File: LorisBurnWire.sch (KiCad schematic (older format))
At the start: 54 parts, among them J1 BurnWire, J2 BurnWire, J3 BurnWire, J4 BurnWire, Q1 BUK7M6R3-40EX, Q2 BUK7M6R3-40EX, Q3 BUK7M6R3-40EX, Q4 BUK7M6R3-40EX, U1 TLC555ID, U2 TLC555ID, U3 LP38501-ADJ, U4 TLC555ID, U5 LMP8646, U6 TLC555ID

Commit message: Added footprint to LMP8646
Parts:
- U5: footprint (none) -> TempoFootprints:SOT-23-THN (DDC)
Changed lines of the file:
@@
 F 0 "U5" H 8200 2000 50  0000 R CNN
 F 1 "LMP8646" H 8300 1925 50  0000 R CNN
-F 2 "" H 8150 1850 50  0001 C CNN
+F 2 "TempoFootprints:SOT-23-THN (DDC)" H 8150 1850 50  0001 C CNN
 F 3 "" H 8150 1850 50  0001 C CNN
 	1    8150 1900

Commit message: added 5v regulator and finished adding footprints
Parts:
- added C16, C17, C18, C19: 22u, Capacitor_SMD:C_1206_3216Metric_Pad1.42x1.75mm_HandSolder, symbol Device:C_Small
- added L1: L_Small, BurnWire:SPM6530T-3R3M, symbol Device:L_Small
- added R22, R24: 100k, Resistor_SMD:R_1206_3216Metric_Pad1.42x1.75mm_HandSolder, symbol Device:R_Small
- added R23: 909k, Resistor_SMD:R_1206_3216Metric_Pad1.42x1.75mm_HandSolder, symbol Device:R_Small
- added U7: RT4812, Package_TO_SOT_SMD:TSOT-23-8_HandSoldering, symbol BurnWireLib:RT4812
- JP1: footprint TempoFootprints:TE_87224-3 -> Connector_PinHeader_2.54mm:PinHeader_1x03_P2.54mm_Vertical
- U3: footprint (none) -> TO_SOT_Packages_SMD:TO-263-5_TabPin3
- U5: footprint TempoFootprints:SOT-23-THN (DDC) -> TO_SOT_Packages_SMD:TSOT-23-6_HandSoldering
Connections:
- net labels removed: 3.5V
- wire segments 219 -> 262
- no-connect marks 0 -> 1
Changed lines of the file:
@@
 F 0 "U3" H 5975 2240 50  0000 C CNN
 F 1 "LP38501-ADJ" H 5975 2149 50  0000 C CNN
-F 2 "" H 5900 2225 50  0001 C CNN
+F 2 "TO_SOT_Packages_SMD:TO-263-5_TabPin3" H 5900 2225 50  0001 C CNN
 F 3 "" H 5900 2225 50  0001 C CNN
 	1    5900 1775
 	1    0    0    -1
 $EndComp
-Wire Wire Line
-	5550 1725 5350 1725
 $Comp
 L Device:C_Small C8
@@
 F 0 "U5" H 8200 2000 50  0000 R CNN
 F 1 "LMP8646" H 8300 1925 50  0000 R CNN
-F 2 "TempoFootprints:SOT-23-THN (DDC)" H 8150 1850 50  0001 C CNN
+F 2 "TO_SOT_Packages_SMD:TSOT-23-6_HandSoldering" H 8150 1850 50  0001 C CNN
 F 3 "" H 8150 1850 50  0001 C CNN
 	1    8150 1900
@@
 Wire Wire Line
 	6775 7850 9125 7850
-Text Label 6650 1575 1    50   ~ 0
-3.5V
 Wire Notes Line
 	10950 700  625  700
@@
 F 0 "JP1" H 5600 2000 50  0000 C CNN
 F 1 "Jumper_3_Open" H 5675 2075 50  0000 C CNN
-F 2 "TempoFootprints:TE_87224-3" H 5350 1875 50  0001 C CNN
+F 2 "Connector_PinHeader_2.54mm:PinHeader_1x03_P2.54mm_Vertical" H 5350 1875 50  0001 C CNN
 F 3 "~" H 5350 1875 50  0001 C CNN
 	1    5350 1875
@@
 Wire Wire Line
 	2350 7850 2350 8150
+$Comp
+L BurnWireLib:RT4812 U7
+U 1 1 5EAF5CE4
+P 2225 1975
+F 0 "U7" H 2275 2390 50  0000 C CNN
+F 1 "RT4812" H 2275 2299 50  0000 C CNN
+F 2 "Package_TO_SOT_SMD:TSOT-23-8_HandSoldering" H 2275 2275 50  0001 C CNN
+F 3 "https://www.digikey.ca/product-detail/en/richtek-usa-inc/RT4812GJ8F/1028-1512-1-ND/5640521" H 2275 2275 50  0001 C CNN
+	1    2225 1975
+	1    0    0    -1
+$EndComp
+$Comp
+L Device:C_Small C16
+U 1 1 5EAF69B3
+P 1425 2000
+F 0 "C16" H 1225 2025 50  0000 L CNN
+F 1 "22u" H 1175 1950 50  0000 L CNN
+F 2 "Capacitor_SMD:C_1206_3216Metric_Pad1.42x1.75mm_HandSolder" H 1425 2000 50  0001 C CNN
+F 3 "~" H 1425 2000 50  0001 C CNN
+	1    1425 2000
+	1    0    0    -1
+$EndComp
+$Comp
+L Device:L_Small L1
+U 1 1 5EB25078
+P 1575 1825
+F 0 "L1" V 1760 1825 50  0000 C CNN
+F 1 "L_Small" V 1669 1825 50  0000 C CNN
+F 2 "BurnWire:SPM6530T-3R3M" H 1575 1825 50  0001 C CNN
+F 3 "~" H 1575 1825 50  0001 C CNN
+F 4 "RICHTEK" H 1575 1825 50  0001 C CNN "MFG Name"
+F 5 "SPM6530T-3R3M" H 1575 1825 50  0001 C CNN "MFG Part Number"
+	1    1575 1825
+	0    -1   -1   0
+$EndComp
+Wire Wire Line
+	1675 1825 1875 1825
+NoConn ~ 1875 2375
+Wire Wire Line
+	1425 1825 1475 1825
+Wire Wire Line
+	1425 1900 1425 1875
+Wire Wire Line
+	1875 2025 1600 2025
+Wire Wire Line
+	1600 2025 1600 1875
+Wire Wire Line
+	1600 1875 1550 1875
+Connection ~ 1425 1875
+Wire Wire Line
+	1425 1875 1425 1825
+$Comp
+L Device:C_Small C17
+U 1 1 5ECA27CF
+P 1550 2175
+F 0 "C17" H 1650 2200 50  0000 L CNN
+F 1 "22u" H 1650 2125 50  0000 L CNN
+F 2 "Capacitor_SMD:C_1206_3216Metric_Pad1.42x1.75mm_HandSolder" H 1550 2175 50  0001 C CNN
+F 3 "~" H 1550 2175 50  0001 C CNN
+	1    1550 2175
+	1    0    0    -1
+$EndComp
+Wire Wire Line
+	1550 2075 1550 1875
+Connection ~ 1550 1875
+Wire Wire Line
+	1550 1875 1425 1875
+Wire Wire Line
+	1550 2275 1550 2725
+Wire Wire Line
+	2325 2725 2325 2625
+Wire Wire Line
+	2275 2575 2275 2625
+Wire Wire Line
+	2275 2625 2325 2625
+Wire Wire Line
+	2375 2575 2375 2625
+Wire Wire Line
+	2375 2625 2325 2625
+Connection ~ 2325 2625
+Wire Wire Line
+	1425 2100 1425 2725
+Wire Wire Line
+	1425 2725 1550 2725
+Connection ~ 1550 2725
+Wire Wire Line
+	1550 2725 1675 2725
+$Comp
+L Device:R_Small R22
+U 1 1 5ED0112A
+P 1675 2500
+F 0 "R22" H 1734 2546 50  0000 L CNN
+F 1 "100k" H 1725 2475 50  0000 L CNN
+F 2 "Resistor_SMD:R_1206_3216Metric_Pad1.42x1.75mm_HandSolder" H 1675 2500 50  0001 C CNN
+F 3 "~" H 1675 2500 50  0001 C CNN
+	1    1675 2500
+	1    0    0    -1
+$EndComp
+Wire Wire Line
+	1675 2400 1675 2275
+Wire Wire Line
+	1675 2275 1875 2275
+Wire Wire Line
+	1675 2600 1675 2725
+Connection ~ 1675 2725
+Wire Wire Line
+	1675 2725 2325 2725
+Wire Wire Line
+	1425 1825 1225 1825
+Connection ~ 1425 1825
+Text GLabel 1225 1825 0    50   Input ~ 0
+PACK+
+$Comp
+L Device:R_Small R23
+U 1 1 5ED480F4
+P 2775 2050
+F 0 "R23" H 2834 2096 50  0000 L CNN
+F 1 "909k" H 2825 2025 50  0000 L CNN
+F 2 "Resistor_SMD:R_1206_3216Metric_Pad1.42x1.75mm_HandSolder" H 2775 2050 50  0001 C CNN
+F 3 "~" H 2775 2050 50  0001 C CNN
+	1    2775 2050
+	1    0    0    -1
+$EndComp
+$Comp
+L Device:R_Small R24
+U 1 1 5ED58F71
+P 2775 2400
+F 0 "R24" H 2834 2446 50  0000 L CNN
+F 1 "100k" H 2825 2375 50  0000 L CNN
+F 2 "Resistor_SMD:R_1206_3216Metric_Pad1.42x1.75mm_HandSolder" H 2775 2400 50  0001 C CNN
+F 3 "~" H 2775 2400 50  0001 C CNN
+	1    2775 2400
+	1    0    0    -1
+$EndComp
+Wire Wire Line
+	2675 1875 2775 1875
+Wire Wire Line
+	2775 1875 2775 1950
+Wire Wire Line
+	2675 2225 2775 2225
+Wire Wire Line
+	2775 2225 2775 2150
+Wire Wire Line
+	2775 2225 2775 2300
+Connection ~ 2775 2225
+Wire Wire Line
+	2775 2500 2775 2725
+Wire Wire Line
+	2775 2725 2325 2725
+Connection ~ 2325 2725
+Connection ~ 2775 1875
+$Comp
+L Device:C_Small C18
+U 1 1 5EDF6398
+P 3175 2175
+F 0 "C18" H 3275 2175 50  0000 L CNN
+F 1 "22u" H 3275 2100 50  0000 L CNN
+F 2 "Capacitor_SMD:C_1206_3216Metric_Pad1.42x1.75mm_HandSolder" H 3175 2175 50  0001 C CNN
+F 3 "~" H 3175 2175 50  0001 C CNN
+	1    3175 2175
+	1    0    0    -1
+$EndComp
+$Comp
+L Device:C_Small C19
+U 1 1 5EE2E4CA
+P 3500 2175
+F 0 "C19" H 3600 2175 50  0000 L CNN
+F 1 "22u" H 3600 2100 50  0000 L CNN
+F 2 "Capacitor_SMD:C_1206_3216Metric_Pad1.42x1.75mm_HandSolder" H 3500 2175 50  0001 C CNN
+F 3 "~" H 3500 2175 50  0001 C CNN
+	1    3500 2175
+	1    0    0    -1
+$EndComp
+Wire Wire Line
+	3175 2000 3175 2075
+Wire Wire Line
+	3500 2000 3500 2075
+Wire Wire Line
+	3175 2275 3175 2450
+Wire Wire Line
+	3500 2450 3500 2275
+Connection ~ 2775 2725
+$Comp
+L power:+5V #PWR0101
+U 1 1 5EECD4F8
+P 3700 1875
+F 0 "#PWR0101" H 3700 1725 50  0001 C CNN
+F 1 "+5V" H 3715 2048 50  0000 C CNN
+F 2 "" H 3700 1875 50  0001 C CNN
+F 3 "" H 3700 1875 50  0001 C CNN
+	1    3700 1875
+	1    0    0    -1
+$EndComp
+Wire Wire Line
+	5350 1725 5550 1725
+Wire Wire Line
+	2775 1875 3325 1875
+Wire Wire Line
+	3175 2000 3325 2000
+Wire Wire Line
+	3175 2450 3325 2450
+Wire Wire Line
+	3325 2450 3325 2725
+Connection ~ 3325 2450
+Wire Wire Line
+	3325 2450 3500 2450
+Wire Wire Line
+	3325 2725 2775 2725
+Wire Wire Line
+	3325 2000 3325 1875
+Connection ~ 3325 2000
+Connection ~ 3325 1875
+Wire Wire Line
+	3325 2000 3500 2000
+Wire Wire Line
+	3325 1875 3700 1875
+$Comp
+L power:GND #PWR0102
+U 1 1 5EF9B6AD
+P 2325 2725
+F 0 "#PWR0102" H 2325 2475 50  0001 C CNN
+F 1 "GND" H 2330 2552 50  0000 C CNN
+F 2 "" H 2325 2725 50  0001 C CNN
+F 3 "" H 2325 2725 50  0001 C CNN
+	1    2325 2725
+	1    0    0    -1
+$EndComp
 $EndSCHEMATC

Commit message: Initial work on PCB layout
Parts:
- D1, D2, D3: footprint Diodes_SMD:D_SOD-123 -> Diode_SMD:D_SOD-123
- U1, U2, U4, U6: footprint Housings_SOIC:SOIC-8_3.9x4.9mm_Pitch1.27mm -> Package_SO:SOIC-8_3.9x4.9mm_P1.27mm
- U3: footprint TO_SOT_Packages_SMD:TO-263-5_TabPin3 -> Package_TO_SOT_SMD:TO-263-5_TabPin3
- U5: footprint TO_SOT_Packages_SMD:TSOT-23-6_HandSoldering -> Package_TO_SOT_SMD:TSOT-23-6_HandSoldering
- U7: symbol BurnWireLib:RT4812 -> LorisBurnWire-rescue:RT4812-BurnWireLib

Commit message: Rough layout of PCB
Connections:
- net PWR_FLAG: now reaches J1.1 (Pin_1), J2.1 (Pin_1), J3.1 (Pin_1), J4.1 (Pin_1)
- net PWR_FLAG: now also R15.1, R18.1, U5.4 (IN-)
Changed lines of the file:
@@
 	1    0    0    -1
 $EndComp
+Text GLabel 9950 1550 3    50   Input ~ 0
+PWR_FLAG
+Text GLabel 5750 7850 3    50   Input ~ 0
+PWR_FLAG
 $EndSCHEMATC

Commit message: edits
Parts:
- added J5: TimerTestPoints, Connector_PinHeader_2.54mm:PinHeader_1x04_P2.54mm_Vertical, symbol Connector:Conn_01x04_Male
- added J6: PACK+, TempoFootprints:TE_282837-2, symbol Connector:Screw_Terminal_01x02
- added J7: TestPointCurrentLimiter, Connector_PinHeader_2.54mm:PinHeader_1x02_P2.54mm_Vertical, symbol Connector:Conn_01x02_Male
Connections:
- net GND: now also J6.2 (Pin_2)
- net PACK+: now also J6.1 (Pin_1)
- net WireCutter1: now also J5.1 (Pin_1)
- net WireCutter2: now also J5.2 (Pin_2)
- net WireCutter3: now also J5.3 (Pin_3)
- net WireCutter4: now also J5.4 (Pin_4)
- net OUT: now reaches C8.2, R18.2, U3.4 (OUT), U5.3 (+IN)
- net OUT: now also J7.2 (Pin_2)
- net PWR_FLAG renamed VS
- net VS: now also J7.1 (Pin_1)
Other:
- moved on the sheet: C1, C10, C11, C14, C16, C17, C18, C19, C2, C3, C4, C5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

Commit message: added simulation
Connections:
- net GND: now also C16.1; no longer C16.2
- net PACK+: now also C16.2, R22.1, U7.7 (EN); no longer C16.1
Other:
- moved on the sheet: C16, C17
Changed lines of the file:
@@
-$EndComp
-$Comp
-L Device:C_Small C16
-U 1 1 5EAF69B3
-P 1425 1725
-F 0 "C16" H 1225 1750 50  0000 L CNN
-F 1 "22u" H 1175 1675 50  0000 L CNN
-F 2 "Capacitor_SMD:C_1206_3216Metric_Pad1.42x1.75mm_HandSolder" H 1425 1725 50  0001 C CNN
-F 3 "~" H 1425 1725 50  0001 C CNN
-	1    1425 1725
-	1    0    0    -1
 $EndComp
 $Comp
@@
 U 1 1 5EB25078
 P 1575 1550
-F 0 "L1" V 1760 1550 50  0000 C CNN
-F 1 "L_Small" V 1669 1550 50  0000 C CNN
+F 0 "L1" V 1750 1475 50  0000 C CNN
+F 1 "L_Small" V 1650 1450 50  0000 C CNN
 F 2 "BurnWire:SPM6530T-3R3M" H 1575 1550 50  0001 C CNN
 F 3 "~" H 1575 1550 50  0001 C CNN
@@
 	1675 1550 1875 1550
 NoConn ~ 1875 2100
-Wire Wire Line
-	1425 1550 1475 1550
-Wire Wire Line
-	1425 1625 1425 1600
-Wire Wire Line
-	1875 1750 1600 1750
-Wire Wire Line
-	1600 1750 1600 1600
-Wire Wire Line
-	1600 1600 1550 1600
-Connection ~ 1425 1600
-Wire Wire Line
-	1425 1600 1425 1550
 $Comp
 L Device:C_Small C17
 U 1 1 5ECA27CF
-P 1550 1900
-F 0 "C17" H 1650 1925 50  0000 L CNN
-F 1 "22u" H 1650 1850 50  0000 L CNN
-F 2 "Capacitor_SMD:C_1206_3216Metric_Pad1.42x1.75mm_HandSolder" H 1550 1900 50  0001 C CNN
-F 3 "~" H 1550 1900 50  0001 C CNN
-	1    1550 1900
-	1    0    0    -1
-$EndComp
-Wire Wire Line
-	1550 1800 1550 1600
-Connection ~ 1550 1600
-Wire Wire Line
-	1550 1600 1425 1600
-Wire Wire Line
-	1550 2000 1550 2450
-Wire Wire Line
-	2325 2450 2325 2350
-Wire Wire Line
-	2275 2300 2275 2350
-Wire Wire Line
-	2275 2350 2325 2350
-Wire Wire Line
-	2375 2300 2375 2350
-Wire Wire Line
-	2375 2350 2325 2350
-Connection ~ 2325 2350
-Wire Wire Line
-	1425 1825 1425 2450
-Wire Wire Line
-	1425 2450 1550 2450
-Connection ~ 1550 2450
-Wire Wire Line
-	1550 2450 1675 2450
+P 1550 1850
+F 0 "C17" H 1625 2075 50  0000 L CNN
+F 1 "22u" H 1625 2000 50  0000 L CNN
+F 2 "Capacitor_SMD:C_1206_3216Metric_Pad1.42x1.75mm_HandSolder" H 1550 1850 50  0001 C CNN
+F 3 "~" H 1550 1850 50  0001 C CNN
+	1    1550 1850
+	1    0    0    -1
+$EndComp
 $Comp
 L Device:R_Small R22
@@
 Wire Wire Line
 	1675 2325 1675 2450
-Connection ~ 1675 2450
-Wire Wire Line
-	1675 2450 2325 2450
-Wire Wire Line
-	1425 1550 1225 1550
-Connection ~ 1425 1550
-Text GLabel 1225 1550 0    50   Input ~ 0
+Text GLabel 950  1550 0    50   Input ~ 0
 PACK+
 $Comp
@@
 	2775 2225 2775 2450
 Wire Wire Line
-	2775 2450 2325 2450
+	2775 2450 2375 2450
 Connection ~ 2325 2450
 Connection ~ 2775 1600
@@
 Wire Wire Line
 	3500 1725 3500 1800
-Wire Wire Line
-	3175 2000 3175 2175
-Wire Wire Line
-	3500 2175 3500 2000
 Connection ~ 2775 2450
 $Comp
@@
 Wire Wire Line
 	3175 1725 3325 1725
-Wire Wire Line
-	3175 2175 3325 2175
-Wire Wire Line
-	3325 2175 3325 2450
-Connection ~ 3325 2175
-Wire Wire Line
-	3325 2175 3500 2175
-Wire Wire Line
-	3325 2450 2775 2450
 Wire Wire Line
 	3325 1725 3325 1600
@@
 Text GLabel 8550 8825 0    50   Input ~ 0
 WireCutter4
+$Comp
+L Device:C_Small C16
+U 1 1 5EAF69B3
+P 1450 1400
+F 0 "C16" H 1225 1475 50  0000 L CNN
+F 1 "22u" H 1225 1375 50  0000 L CNN
+F 2 "Capacitor_SMD:C_1206_3216Metric_Pad1.42x1.75mm_HandSolder" H 1450 1400 50  0001 C CNN
+F 3 "~" H 1450 1400 50  0001 C CNN
+	1    1450 1400
+	1    0    0    -1
+$EndComp
+Wire Wire Line
+	1450 1750 1450 1550
+Wire Wire Line
+	1450 1750 1550 1750
+Connection ~ 1450 1550
+Wire Wire Line
+	1450 1550 1475 1550
+Wire Wire Line
+	1675 2000 1375 2000
+Wire Wire Line
+	1375 2000 1375 1550
+Connection ~ 1675 2000
+Connection ~ 1375 1550
+Wire Wire Line
+	1375 1550 1450 1550
+Connection ~ 1550 1750
+Wire Wire Line
+	1550 1750 1875 1750
+Wire Wire Line
+	2275 2300 2275 2450
+Wire Wire Line
+	1675 2450 2275 2450
+Connection ~ 2275 2450
+Wire Wire Line
+	2275 2450 2325 2450
+Wire Wire Line
+	2375 2300 2375 2450
+Connection ~ 2375 2450
+Wire Wire Line
+	2375 2450 2325 2450
+Wire Wire Line
+	1550 1950 1700 1950
+Wire Wire Line
+	1700 1950 1700 1925
+$Comp
+L power:GND #PWR?
+U 1 1 5F0BE645
+P 1700 1925
+F 0 "#PWR?" H 1700 1675 50  0001 C CNN
+F 1 "GND" H 1700 1800 50  0000 C CNN
+F 2 "" H 1700 1925 50  0001 C CNN
+F 3 "" H 1700 1925 50  0001 C CNN
+	1    1700 1925
+	-1   0    0    1
+$EndComp
+Wire Wire Line
+	950  1550 1375 1550
+$Comp
+L power:GND #PWR?
+U 1 1 5F15D96B
+P 1475 1200
+F 0 "#PWR?" H 1475 950 50  0001 C CNN
+F 1 "GND" V 1475 1025 50  0000 C CNN
+F 2 "" H 1475 1200 50  0001 C CNN
+F 3 "" H 1475 1200 50  0001 C CNN
+	1    1475 1200
+	0    -1   -1   0
+$EndComp
+Wire Wire Line
+	1450 1550 1450 1500
+Wire Wire Line
+	1450 1300 1450 1200
+Wire Wire Line
+	1450 1200 1475 1200
+Wire Wire Line
+	3175 2000 3175 2450
+Connection ~ 3175 2450
+Wire Wire Line
+	3175 2450 2775 2450
+Wire Wire Line
+	3500 2000 3500 2450
+Wire Wire Line
+	3175 2450 3500 2450
 $EndSCHEMATC

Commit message: changes for owen
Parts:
- removed C1, C10, C11, C3, C4, C6, C7: 0.01uF, Capacitor_SMD:C_1206_3216Metric_Pad1.42x1.75mm_HandSolder, symbol Device:C
- removed C14, C2, C5, C9: 10uF, Capacitor_SMD:C_1206_3216Metric_Pad1.42x1.75mm_HandSolder, symbol Device:C
- removed C16, C17, C18, C19: 22u, Capacitor_SMD:C_1206_3216Metric_Pad1.42x1.75mm_HandSolder, symbol Device:C_Small
- removed D1, D2, D3: 1N4148W-13-F, Diode_SMD:D_SOD-123, symbol Device:D
- removed J5: TimerTestPoints, Connector_PinHeader_2.54mm:PinHeader_1x04_P2.54mm_Vertical, symbol Connector:Conn_01x04_Male
- removed J6: PACK+, TempoFootprints:TE_282837-2, symbol Connector:Screw_Terminal_01x02
- removed L1: L_Small, BurnWire:SPM6530T-3R3M, symbol Device:L_Small
- removed R10, R17, R7: 33K, Resistor_SMD:R_1206_3216Metric_Pad1.42x1.75mm_HandSolder, symbol Device:R_US
- removed R13, R21, R5, R8: 2.73 M, Resistor_SMD:R_1206_3216Metric_Pad1.42x1.75mm_HandSolder, symbol Device:R_US
- removed R22, R24: 100k, Resistor_SMD:R_1206_3216Metric_Pad1.42x1.75mm_HandSolder, symbol Device:R_Small
- removed R23: 909k, Resistor_SMD:R_1206_3216Metric_Pad1.42x1.75mm_HandSolder, symbol Device:R_Small
- removed R3: 5M, Resistor_SMD:R_1206_3216Metric_Pad1.42x1.75mm_HandSolder, symbol Device:R_US
- removed U1, U2, U4, U6: TLC555ID, Package_SO:SOIC-8_3.9x4.9mm_P1.27mm, symbol LorisBurnWire-rescue:TLC555-Loris
- removed U7: RT4812, Package_TO_SOT_SMD:TSOT-23-8_HandSoldering, symbol LorisBurnWire-rescue:RT4812-BurnWireLib
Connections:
- no-connect marks 1 -> 0
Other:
- note removed: "5v Regulator"
- note removed: "Monostable sequential timer"
- moved on the sheet: C12, C13, C15, C8, J7, JP1, R12, R14, R15, R16, R18, U3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

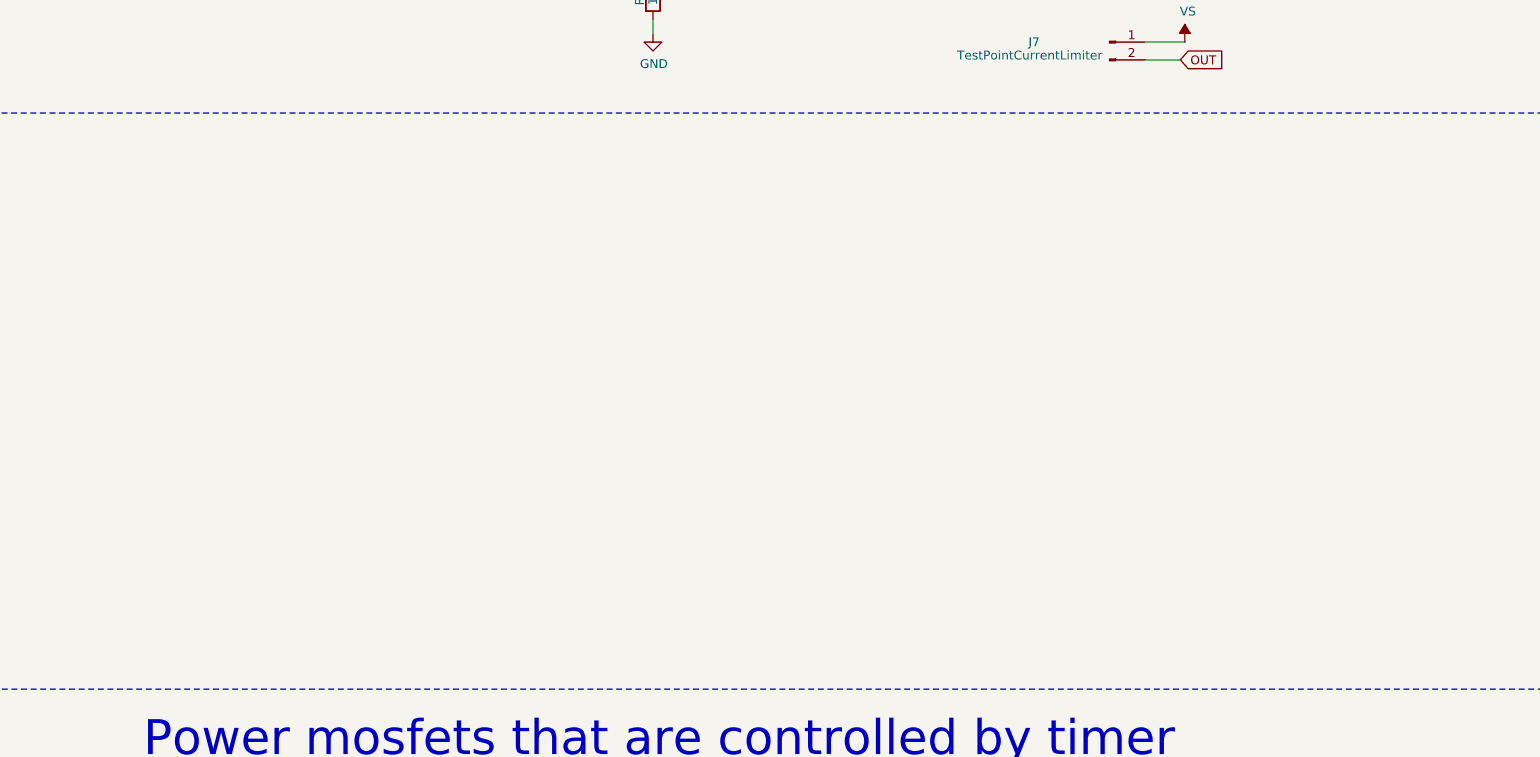
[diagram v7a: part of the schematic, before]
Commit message: New Timer Schematic based on LTC6993
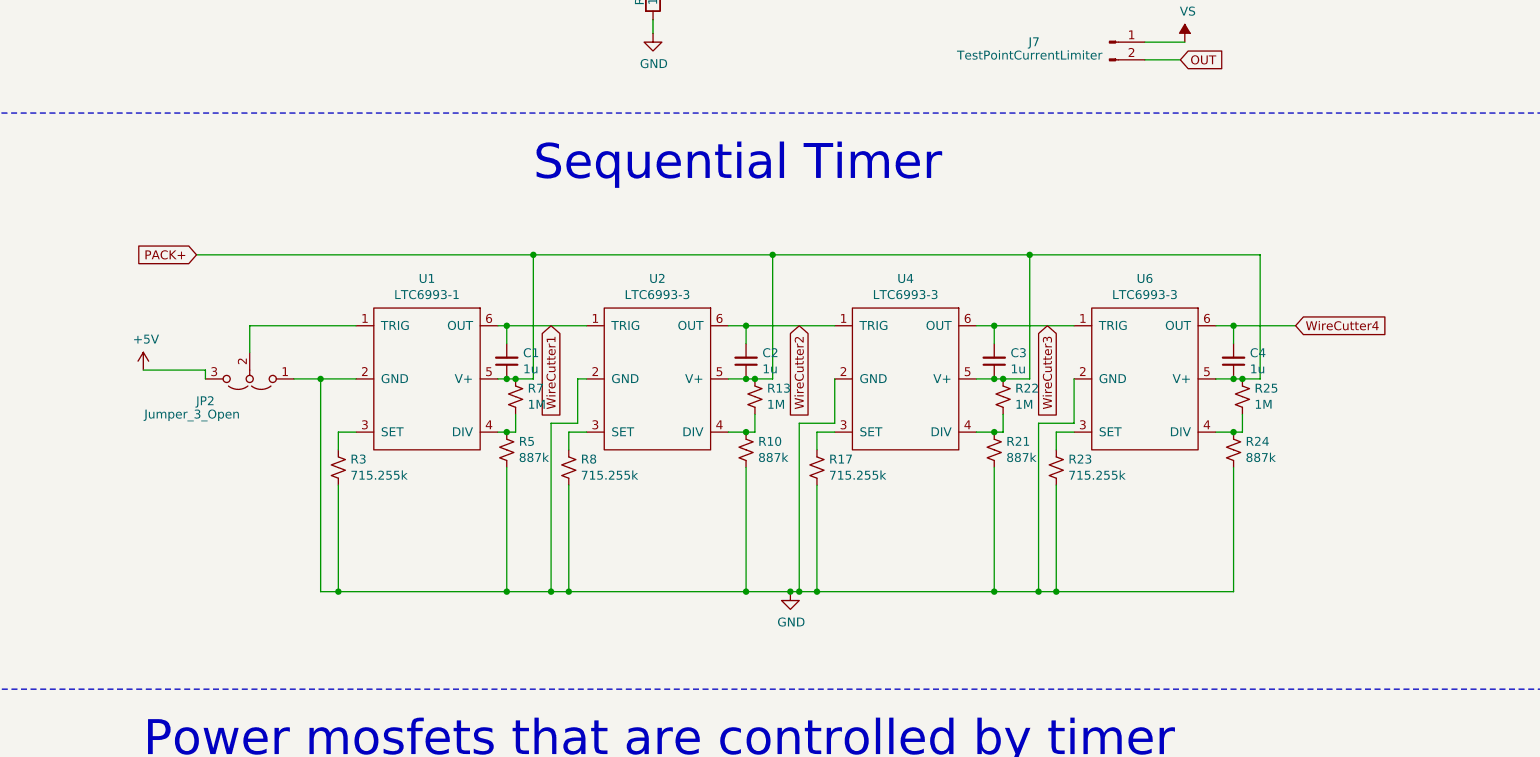
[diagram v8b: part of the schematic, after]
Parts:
- added C1, C2, C3, C4: 1u, Capacitor_SMD:C_1206_3216Metric_Pad1.42x1.75mm_HandSolder, symbol Device:C_Small
- added JP2: Jumper_3_Open, Connector_PinHeader_2.54mm:PinHeader_1x03_P2.54mm_Vertical, symbol Jumper:Jumper_3_Open
- added R10, R21, R24, R5: 887k, symbol Device:R_Small_US
- added R13, R22, R25, R7: 1M, symbol Device:R_Small_US
- added R17, R23, R3, R8: 715.255k, symbol Device:R_Small_US
- added U1: LTC6993-1, Package_TO_SOT_SMD:TSOT-23-6_HandSoldering, symbol Loris:LTC6993-1
- added U2, U4, U6: LTC6993-3, Package_TO_SOT_SMD:TSOT-23-6_HandSoldering, symbol Loris:LTC6993-3
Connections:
- net +5V: now also JP2.3 (B)
- net GND: now also JP2.1 (A), R10.2, R17.2, R21.2, R23.2, R24.2, R3.2, R5.2, R8.2, U1.2 (GND), U2.2 (GND), U4.2 (GND), U6.2 (GND)
- net PACK+: now also C1.1, C2.1, C3.1, C4.1, R13.1, R22.1, R25.1, R7.1, U1.5 (V+), U2.5 (V+), U4.5 (V+), U6.5 (V+)
- net WireCutter1: now also C1.2, U1.6 (OUT), U2.1 (TRIG)
- net WireCutter2: now also C2.2, U2.6 (OUT), U4.1 (TRIG)
- net WireCutter3: now also C3.2, U4.6 (OUT), U6.1 (TRIG)
- net WireCutter4: now also C4.2, U6.6 (OUT)
- new net: JP2.2 (C), U1.1 (TRIG)
- new net: R3.1, U1.3 (SET)
- new net: R5.1, R7.2, U1.4 (DIV)
- new net: R8.1, U2.3 (SET)
- new net: R10.1, R13.2, U2.4 (DIV)
- new net: R17.1, U4.3 (SET)
- new net: R21.1, R22.2, U4.4 (DIV)
- new net: R23.1, U6.3 (SET)
- new net: R24.1, R25.2, U6.4 (DIV)
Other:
- note added: "Sequential Timer"
